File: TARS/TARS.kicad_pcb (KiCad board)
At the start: 2 copper layers, 48.4 x 75.6 mm, 96 parts, among them J1 Display header, J11 Conn_01x03_Pin, J12 Receptacle side, J13 Main board side, J14 Conn_01x06_Pin, J15 Conn_01x06_Pin, J16 Conn_01x04_Pin, J17 Conn_01x04_Pin, J2 Conn_01x04_Pin, J3 USB_C_Receptacle_USB2.0_16P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

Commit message: update mousebites
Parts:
- removed ? (x49): , 
- added mouse-bite-2mm-slot: VAL**, Panelization:mouse-bite-2mm-slot, F.Cu at (164.8, 105.5)
- added mouse-bite-2mm-slot: VAL**, Panelization:mouse-bite-2mm-slot, F.Cu at (164.8, 122.0)
- added mouse-bite-2mm-slot: VAL**, Panelization:mouse-bite-2mm-slot, F.Cu at (164.8, 83.8)
- added mouse-bite-2mm-slot: VAL**, Panelization:mouse-bite-2mm-slot, F.Cu at (164.8, 150.2)
- moved D1 0.66 mm to (175.9, 154.3)
- moved D3 0.66 mm to (168.6, 150.7)
- moved D5 0.66 mm to (175.9, 141.0)
- moved D8 0.66 mm to (175.9, 131.4)
- moved D9 0.66 mm to (175.9, 125.4)
- moved D10 0.66 mm to (172.2, 125.4)
- moved D11 0.66 mm to (172.2, 121.7)
- moved D12 0.66 mm to (168.6, 121.8)
- moved J12 0.66 mm to (167.8, 82.7)
- moved J3 0.66 mm to (167.7, 111.7)
- moved J5 0.66 mm to (175.6, 117.6)
- moved D2 0.66 mm to (172.2, 150.7)
- moved D6 0.66 mm to (168.6, 141.0)
- moved R15 0.66 mm to (168.8, 97.8)
- moved R16 0.66 mm to (168.8, 100.7)
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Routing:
- net +3V3: track 51.5 -> 63.5 mm, vias 8 -> 10
- net BCLK: track 34.1 -> 35.1 mm
- net FCLK: track 36.1 -> 37.0 mm
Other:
- board size 48.4 x 75.6 mm -> 48 x 75.6 mm

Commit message: update gerbers and readme
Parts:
- moved SW1 16.9 mm to (145.1, 138.2), turned to 45 degrees
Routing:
- net RIGHT: track 11.2 -> 24.6 mm
- net DOWN: track 37.4 -> 26.1 mm
- net +3V3: track 63.5 -> 52.3 mm, vias 10 -> 11
- net ENTER: track 19.9 -> 9.73 mm
- net LEFT: track 22.7 -> 17.5 mm

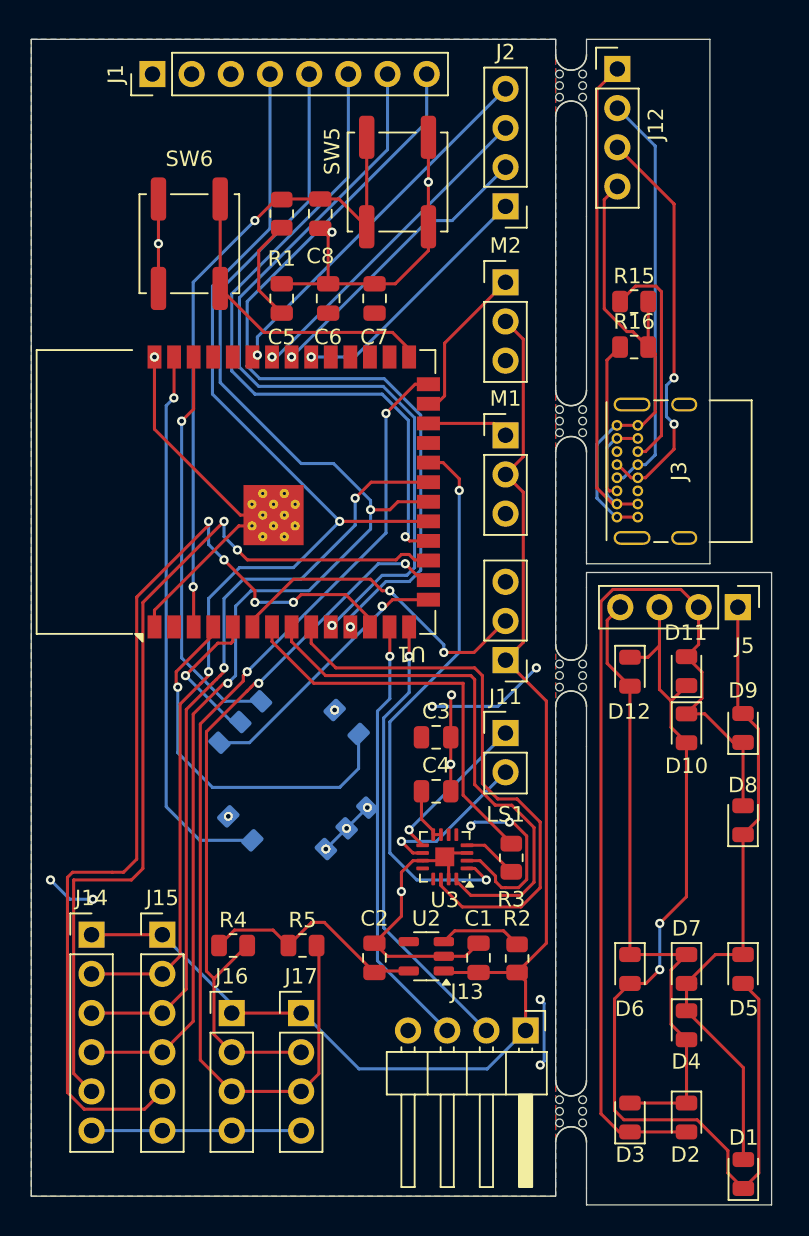
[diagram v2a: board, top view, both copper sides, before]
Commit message: update pcb (remove mouse bites)
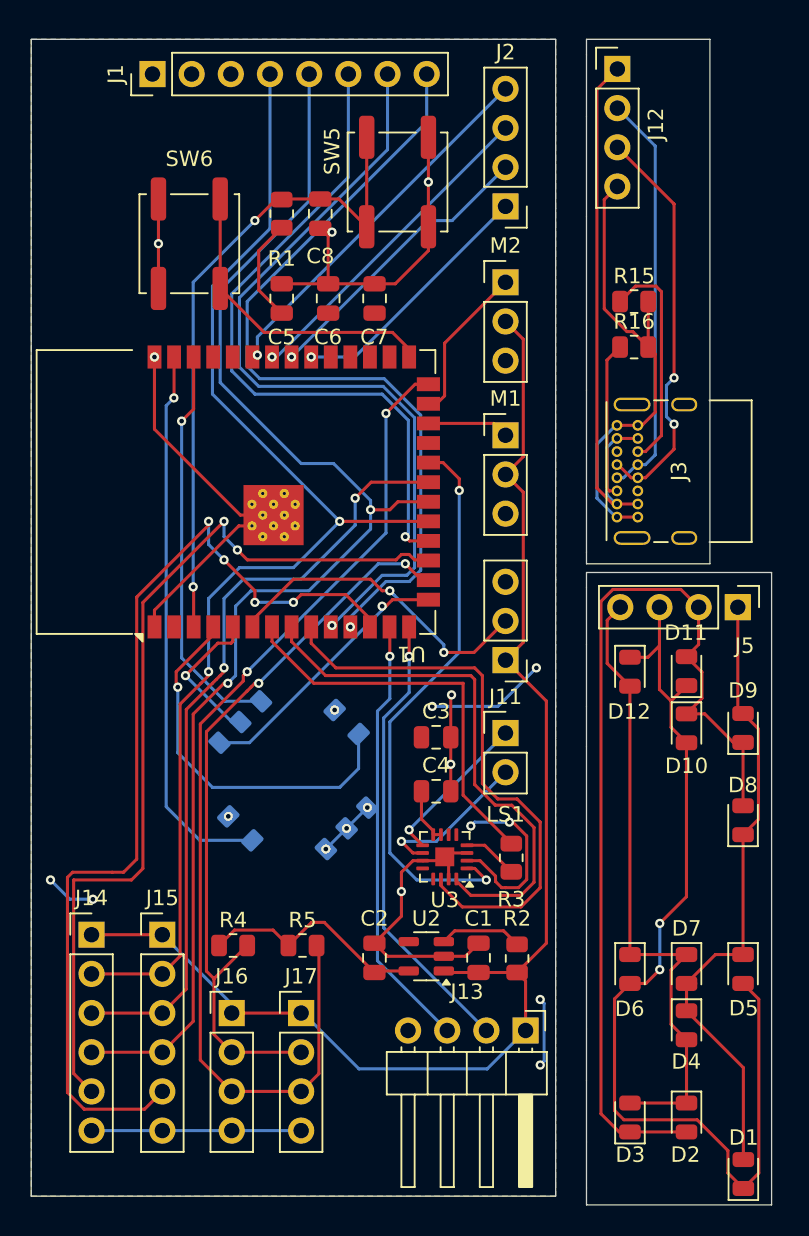
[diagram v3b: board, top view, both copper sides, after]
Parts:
- removed mouse-bite-2mm-slot (x4): VAL**, Panelization:mouse-bite-2mm-slot

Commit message: pcb silkscreen separation
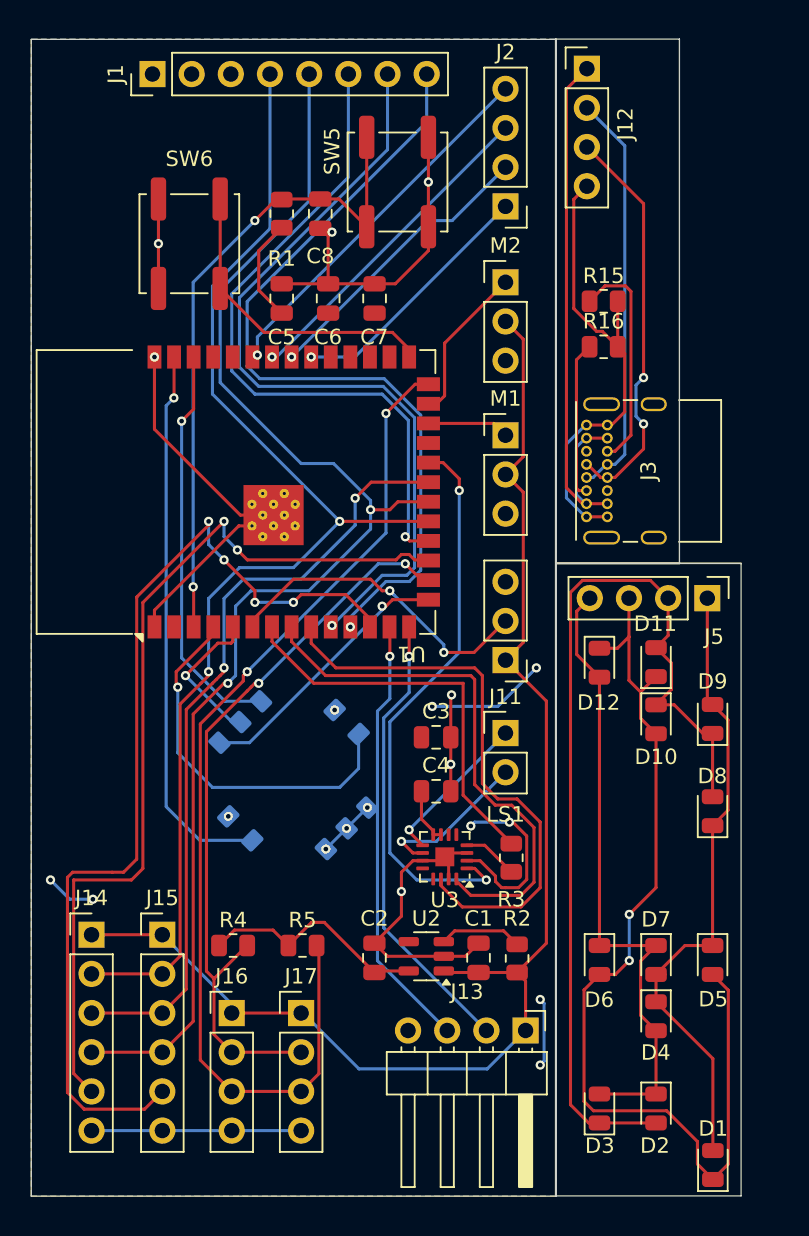
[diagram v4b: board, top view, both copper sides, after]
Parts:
- moved D1 2.06 mm to (173.9, 153.7)
- moved D2 2.06 mm to (170.3, 150.1)
- moved D3 2.06 mm to (166.6, 150.1)
- moved D8 2.06 mm to (173.9, 130.8)
- moved D10 2.06 mm to (170.3, 124.8)
- moved D12 2.06 mm to (166.6, 121.2)
- moved D9 2.06 mm to (173.9, 124.8)
- moved J5 2.06 mm to (173.6, 117.0)
- moved D11 2.06 mm to (170.3, 121.1)
- moved D4 2.06 mm to (170.3, 144.1)
- moved D5 2.06 mm to (173.9, 140.4)
- moved D6 2.06 mm to (166.6, 140.4)
- moved D7 2.06 mm to (170.3, 140.4)
- moved J12 1.98 mm to (165.8, 82.7)
- moved J3 1.98 mm to (165.8, 111.7)
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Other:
- board size 48 x 75.6 mm -> 46 x 75 mm
